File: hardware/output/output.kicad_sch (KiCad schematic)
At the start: 100 parts, among them J1 AudioJack2_SwitchT, J2 AudioJack2_SwitchT, J3 AudioJack2_SwitchT, J4 AudioJack2_SwitchT, J5 Conn_02x08_Odd_Even, J6 AudioJack3, J7 Conn_02x08_Odd_Even, J8 Conn_02x08_Odd_Even, Q1 2N3906, Q2 2N3904, Q3 2N3906, Q4 2N3904, U1 TL074, U2 LM386, U3 LM386

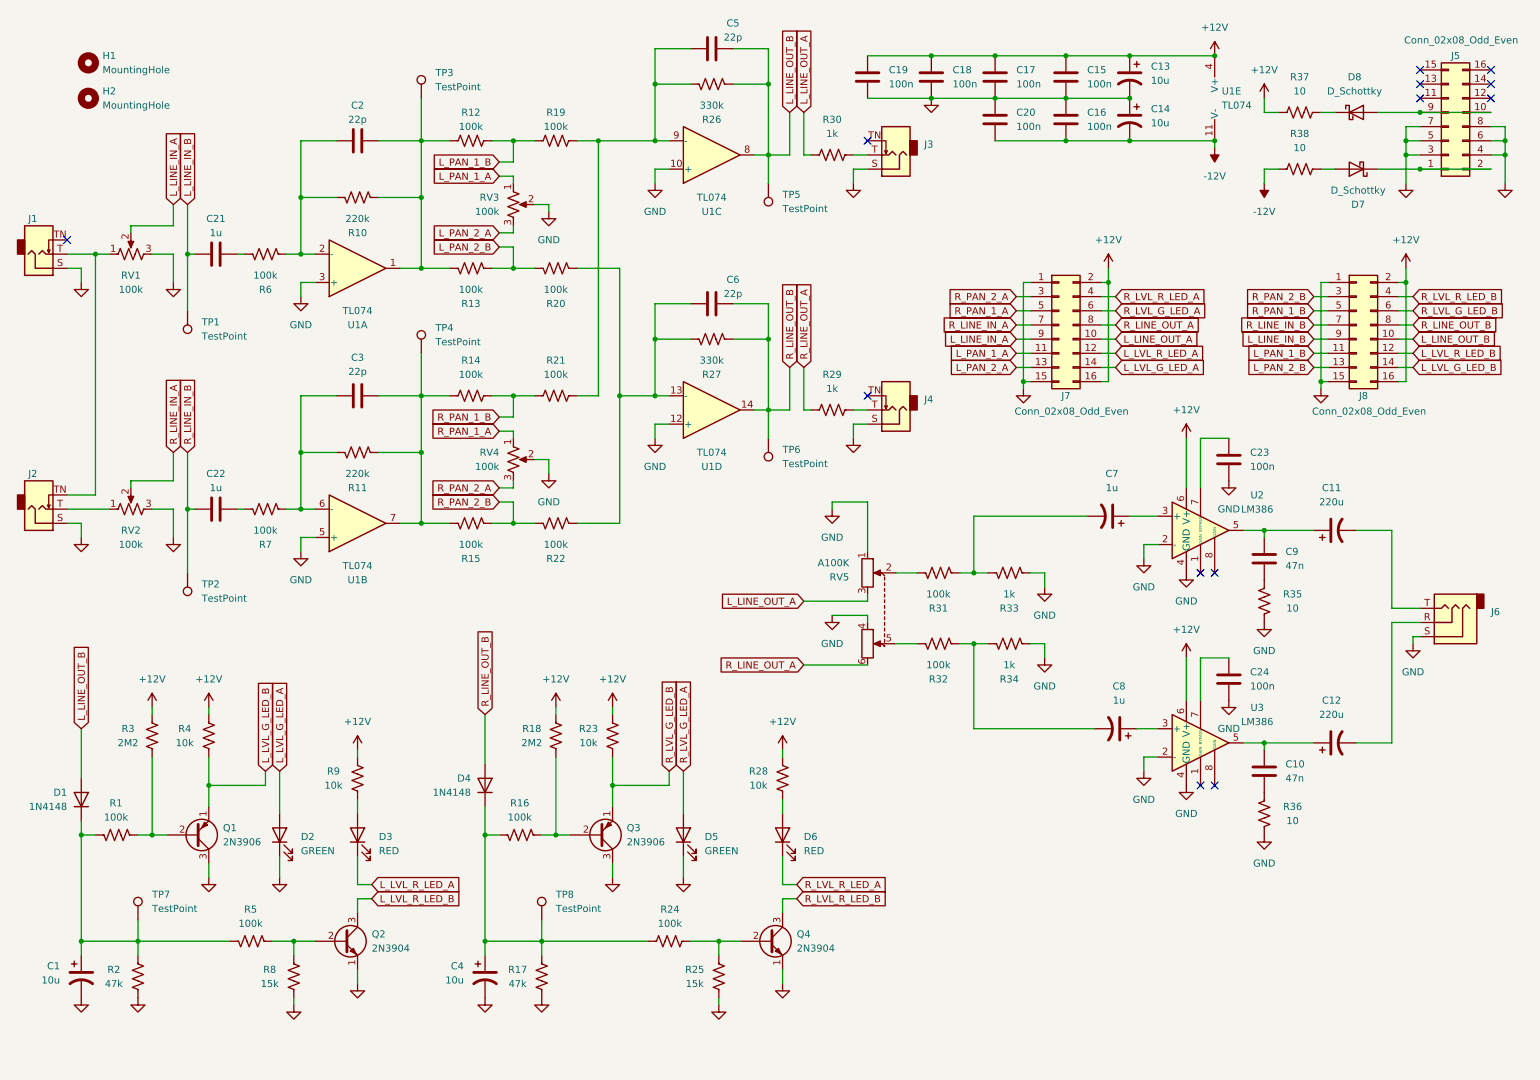
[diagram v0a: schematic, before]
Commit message: v2 board: SMT components, upgraded OPA1688 amplifier
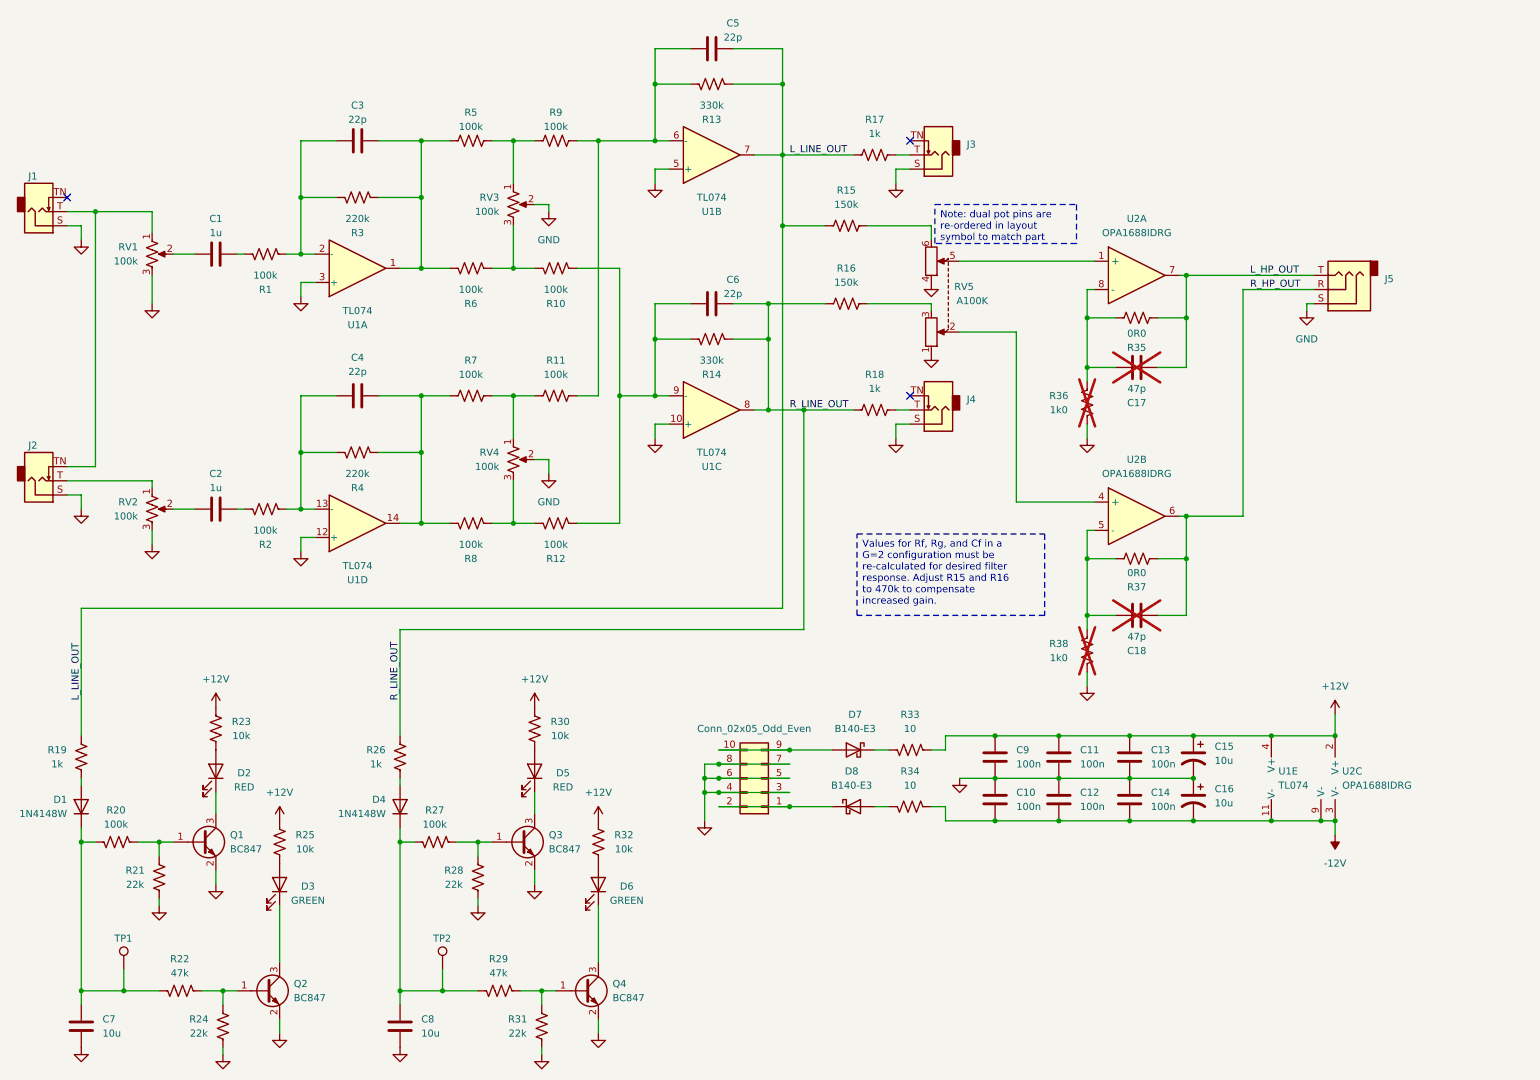
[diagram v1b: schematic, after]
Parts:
- removed C1, C4: 10u, Capacitor_THT:CP_Radial_D4.0mm_P2.00mm, symbol Device:C_Polarized_US
- removed C10, C9: 47n, Capacitor_THT:C_Disc_D5.0mm_W2.5mm_P2.50mm, symbol Device:C
- removed C11, C12: 220u, Capacitor_THT:CP_Radial_D6.3mm_P2.50mm, symbol Device:C_Polarized_US
- removed C23, C24: 100n, Capacitor_THT:C_Disc_D5.0mm_W2.5mm_P2.50mm, symbol Device:C
- removed C7: 1u, Capacitor_THT:C_Disc_D5.0mm_W2.5mm_P5.00mm, symbol Device:C_Polarized_US
- removed C8: 1u, Capacitor_THT:C_Disc_D5.0mm_W2.5mm_P2.50mm, symbol Device:C_Polarized_US
- removed D1: 1N4148, Diode_THT:D_DO-35_SOD27_P7.62mm_Horizontal, symbol Diode:1N4148
- removed D2: GREEN, LED_THT:LED_D3.0mm_Clear, symbol Device:LED
- removed D4: 1N4148, Diode_THT:D_DO-35_SOD27_P2.54mm_Vertical_AnodeUp, symbol Diode:1N4148
- removed D7, D8: D_Schottky, Diode_THT:D_DO-41_SOD81_P7.62mm_Horizontal, symbol Device:D_Schottky
- removed H1, H2: MountingHole, MountingHole:MountingHole_3.2mm_M3_DIN965, symbol Mechanical:MountingHole
- removed J5: Conn_02x08_Odd_Even, Connector_IDC:IDC-Header_2x08_P2.54mm_Vertical, symbol Connector_Generic:Conn_02x08_Odd_Even
- removed J7, J8: Conn_02x08_Odd_Even, Custom_PinHeader_P2.54mm:PinHeader_2x08_P2.54mm_Vertical_ThinPad, symbol Connector_Generic:Conn_02x08_Odd_Even
- removed Q1, Q3: 2N3906, Package_TO_SOT_THT:TO-92_Inline_Wide, symbol Transistor_BJT:2N3906
- removed Q2, Q4: 2N3904, Package_TO_SOT_THT:TO-92_Inline_Wide, symbol Transistor_BJT:2N3904
- removed R1: 100k, Resistor_THT:R_Axial_DIN0204_L3.6mm_D1.6mm_P2.54mm_Vertical, symbol Device:R_US
- removed R17, R2: 47k, Resistor_THT:R_Axial_DIN0204_L3.6mm_D1.6mm_P2.54mm_Vertical, symbol Device:R_US
- removed R18, R3: 2M2, Resistor_THT:R_Axial_DIN0204_L3.6mm_D1.6mm_P2.54mm_Vertical, symbol Device:R_US
- removed R23, R4: 10k, Resistor_THT:R_Axial_DIN0204_L3.6mm_D1.6mm_P2.54mm_Vertical, symbol Device:R_US
- removed R33, R34: 1k, Resistor_THT:R_Axial_DIN0204_L3.6mm_D1.6mm_P2.54mm_Vertical, symbol Device:R_US
- removed TP1, TP3, TP4, TP5, TP6, TP8: TestPoint, Connector_PinHeader_2.54mm:PinHeader_1x01_P2.54mm_Vertical, symbol Connector:TestPoint
- removed U2, U3: LM386, Package_DIP:DIP-8_W7.62mm_Socket, symbol Amplifier_Audio:LM386
- added C17, C18: 47p, Capacitor_SMD:C_0805_2012Metric_Pad1.18x1.45mm_HandSolder, symbol Device:C
- added C7, C8: 10u, Capacitor_SMD:C_0805_2012Metric_Pad1.18x1.45mm_HandSolder, symbol Device:C
- added D1, D4: 1N4148W, Diode_SMD:D_SOD-123, symbol Diode:1N4148W
- added D3: GREEN, LED_THT:LED_D3.0mm_Clear, symbol Device:LED
- added D7, D8: B140-E3, Diode_SMD:D_SMA, symbol Diode:B140-E3
- added J6: Conn_02x05_Odd_Even, Connector_IDC:IDC-Header_2x05_P2.54mm_Vertical, symbol Connector_Generic:Conn_02x05_Odd_Even
- added Q1, Q2, Q3, Q4: BC847, Package_TO_SOT_SMD:SOT-23, symbol Transistor_BJT:BC847
- added R15: 150k, Resistor_SMD:R_0805_2012Metric_Pad1.20x1.40mm_HandSolder, symbol Device:R_US
- added R19, R26: 1k, Resistor_SMD:R_0805_2012Metric_Pad1.20x1.40mm_HandSolder, symbol Device:R_US
- added R22, R29: 47k, Resistor_SMD:R_0805_2012Metric_Pad1.20x1.40mm_HandSolder, symbol Device:R_US
- added R27: 100k, Resistor_SMD:R_0805_2012Metric_Pad1.20x1.40mm_HandSolder, symbol Device:R_US
- added R30: 10k, Resistor_SMD:R_0805_2012Metric_Pad1.20x1.40mm_HandSolder, symbol Device:R_US
- added R37: 0R0, Resistor_SMD:R_0805_2012Metric_Pad1.20x1.40mm_HandSolder, symbol Device:R_US
- added R38: 1k0, Resistor_SMD:R_0805_2012Metric_Pad1.20x1.40mm_HandSolder, symbol Device:R_US
- added U2: OPA1688IDRG, Package_SON:WSON-8-1EP_3x3mm_P0.5mm_EP1.2x2mm, symbol AudioICs:OPA1688IDRG
- C1: renamed from C21; footprint Capacitor_THT:C_Disc_D5.0mm_W2.5mm_P2.50mm -> Capacitor_SMD:C_0805_2012Metric_Pad1.18x1.45mm_HandSolder
- C10: renamed from C19; footprint Capacitor_THT:C_Disc_D5.0mm_W2.5mm_P5.00mm -> Capacitor_SMD:C_0805_2012Metric_Pad1.18x1.45mm_HandSolder
- C11: renamed from C17; footprint Capacitor_THT:C_Disc_D5.0mm_W2.5mm_P2.50mm -> Capacitor_SMD:C_0805_2012Metric_Pad1.18x1.45mm_HandSolder
- C12: renamed from C20; footprint Capacitor_THT:C_Disc_D5.0mm_W2.5mm_P5.00mm -> Capacitor_SMD:C_0805_2012Metric_Pad1.18x1.45mm_HandSolder
- C13: renamed from C15; footprint Capacitor_THT:C_Disc_D5.0mm_W2.5mm_P2.50mm -> Capacitor_SMD:C_0805_2012Metric_Pad1.18x1.45mm_HandSolder
- C14: renamed from C16; footprint Capacitor_THT:C_Disc_D5.0mm_W2.5mm_P2.50mm -> Capacitor_SMD:C_0805_2012Metric_Pad1.18x1.45mm_HandSolder
- C15: renamed from C13; footprint Capacitor_THT:CP_Radial_D4.0mm_P2.00mm -> Capacitor_THT:CP_Radial_D5.0mm_P2.00mm
- C16: renamed from C14; footprint Capacitor_THT:CP_Radial_D4.0mm_P2.00mm -> Capacitor_THT:CP_Radial_D5.0mm_P2.00mm
- C2: renamed from C22; footprint Capacitor_THT:C_Disc_D5.0mm_W2.5mm_P2.50mm -> Capacitor_SMD:C_0805_2012Metric_Pad1.18x1.45mm_HandSolder
- C3: renamed from C2; footprint Capacitor_THT:C_Disc_D5.0mm_W2.5mm_P2.50mm -> Capacitor_SMD:C_0805_2012Metric_Pad1.18x1.45mm_HandSolder
- C4: renamed from C3; footprint Capacitor_THT:C_Disc_D5.0mm_W2.5mm_P2.50mm -> Capacitor_SMD:C_0805_2012Metric_Pad1.18x1.45mm_HandSolder
- C5, C6: footprint Capacitor_THT:C_Disc_D5.0mm_W2.5mm_P2.50mm -> Capacitor_SMD:C_0805_2012Metric_Pad1.18x1.45mm_HandSolder
- C9: renamed from C18; footprint Capacitor_THT:C_Disc_D5.0mm_W2.5mm_P2.50mm -> Capacitor_SMD:C_0805_2012Metric_Pad1.18x1.45mm_HandSolder
- D5: value GREEN -> RED
- D6: value RED -> GREEN
- J1, J2, J3, J4: footprint AudioJacks:Jack_3.5mm_QingPu_WQP-PJ301M-12_Vertical -> AudioJacks:Jack_3.5mm_QingPu_WQP-PJ301M-12_Vertical_Slim
- R1: renamed from R6; footprint Resistor_THT:R_Axial_DIN0207_L6.3mm_D2.5mm_P7.62mm_Horizontal -> Resistor_SMD:R_0805_2012Metric_Pad1.20x1.40mm_HandSolder
- R10: renamed from R20; footprint Resistor_THT:R_Axial_DIN0204_L3.6mm_D1.6mm_P2.54mm_Vertical -> Resistor_SMD:R_0805_2012Metric_Pad1.20x1.40mm_HandSolder
- R11: renamed from R21; footprint Resistor_THT:R_Axial_DIN0204_L3.6mm_D1.6mm_P2.54mm_Vertical -> Resistor_SMD:R_0805_2012Metric_Pad1.20x1.40mm_HandSolder
- R12: renamed from R22; footprint Resistor_THT:R_Axial_DIN0207_L6.3mm_D2.5mm_P7.62mm_Horizontal -> Resistor_SMD:R_0805_2012Metric_Pad1.20x1.40mm_HandSolder
- R13: renamed from R26; footprint Resistor_THT:R_Axial_DIN0204_L3.6mm_D1.6mm_P2.54mm_Vertical -> Resistor_SMD:R_0805_2012Metric_Pad1.20x1.40mm_HandSolder
- R14: renamed from R27; footprint Resistor_THT:R_Axial_DIN0204_L3.6mm_D1.6mm_P2.54mm_Vertical -> Resistor_SMD:R_0805_2012Metric_Pad1.20x1.40mm_HandSolder
- R16: value 100k -> 150k; footprint Resistor_THT:R_Axial_DIN0204_L3.6mm_D1.6mm_P2.54mm_Vertical -> Resistor_SMD:R_0805_2012Metric_Pad1.20x1.40mm_HandSolder
- R17: renamed from R30; footprint Resistor_THT:R_Axial_DIN0204_L3.6mm_D1.6mm_P2.54mm_Vertical -> Resistor_SMD:R_0805_2012Metric_Pad1.20x1.40mm_HandSolder
- R18: renamed from R29; footprint Resistor_THT:R_Axial_DIN0204_L3.6mm_D1.6mm_P2.54mm_Vertical -> Resistor_SMD:R_0805_2012Metric_Pad1.20x1.40mm_HandSolder
- R2: renamed from R7; footprint Resistor_THT:R_Axial_DIN0204_L3.6mm_D1.6mm_P2.54mm_Vertical -> Resistor_SMD:R_0805_2012Metric_Pad1.20x1.40mm_HandSolder
- R20: renamed from R5; footprint Resistor_THT:R_Axial_DIN0204_L3.6mm_D1.6mm_P2.54mm_Vertical -> Resistor_SMD:R_0805_2012Metric_Pad1.20x1.40mm_HandSolder
- R21: renamed from R8; value 15k -> 22k; footprint Resistor_THT:R_Axial_DIN0204_L3.6mm_D1.6mm_P2.54mm_Vertical -> Resistor_SMD:R_0805_2012Metric_Pad1.20x1.40mm_HandSolder
- R23: renamed from R9; footprint Resistor_THT:R_Axial_DIN0204_L3.6mm_D1.6mm_P2.54mm_Vertical -> Resistor_SMD:R_0805_2012Metric_Pad1.20x1.40mm_HandSolder
- R24, R31: value 100k -> 22k; footprint Resistor_THT:R_Axial_DIN0204_L3.6mm_D1.6mm_P2.54mm_Vertical -> Resistor_SMD:R_0805_2012Metric_Pad1.20x1.40mm_HandSolder
- R25: value 15k -> 10k; footprint Resistor_THT:R_Axial_DIN0204_L3.6mm_D1.6mm_P2.54mm_Vertical -> Resistor_SMD:R_0805_2012Metric_Pad1.20x1.40mm_HandSolder
- R28: value 10k -> 22k; footprint Resistor_THT:R_Axial_DIN0204_L3.6mm_D1.6mm_P2.54mm_Vertical -> Resistor_SMD:R_0805_2012Metric_Pad1.20x1.40mm_HandSolder
- R3: renamed from R10; footprint Resistor_THT:R_Axial_DIN0204_L3.6mm_D1.6mm_P2.54mm_Vertical -> Resistor_SMD:R_0805_2012Metric_Pad1.20x1.40mm_HandSolder
- R32: value 100k -> 10k; footprint Resistor_THT:R_Axial_DIN0204_L3.6mm_D1.6mm_P2.54mm_Vertical -> Resistor_SMD:R_0805_2012Metric_Pad1.20x1.40mm_HandSolder
- R33: renamed from R37; footprint Resistor_THT:R_Axial_DIN0207_L6.3mm_D2.5mm_P7.62mm_Horizontal -> Resistor_SMD:R_0805_2012Metric_Pad1.20x1.40mm_HandSolder
- R34: renamed from R38; footprint Resistor_THT:R_Axial_DIN0207_L6.3mm_D2.5mm_P7.62mm_Horizontal -> Resistor_SMD:R_0805_2012Metric_Pad1.20x1.40mm_HandSolder
- R35: value 10 -> 0R0; footprint Resistor_THT:R_Axial_DIN0204_L3.6mm_D1.6mm_P2.54mm_Vertical -> Resistor_SMD:R_0805_2012Metric_Pad1.20x1.40mm_HandSolder
- R36: value 10 -> 1k0; footprint Resistor_THT:R_Axial_DIN0204_L3.6mm_D1.6mm_P2.54mm_Vertical -> Resistor_SMD:R_0805_2012Metric_Pad1.20x1.40mm_HandSolder; now not fitted
- R4: renamed from R11; footprint Resistor_THT:R_Axial_DIN0204_L3.6mm_D1.6mm_P2.54mm_Vertical -> Resistor_SMD:R_0805_2012Metric_Pad1.20x1.40mm_HandSolder
- R5: renamed from R12; footprint Resistor_THT:R_Axial_DIN0204_L3.6mm_D1.6mm_P2.54mm_Vertical -> Resistor_SMD:R_0805_2012Metric_Pad1.20x1.40mm_HandSolder
- R6: renamed from R13; footprint Resistor_THT:R_Axial_DIN0204_L3.6mm_D1.6mm_P2.54mm_Vertical -> Resistor_SMD:R_0805_2012Metric_Pad1.20x1.40mm_HandSolder
- R7: renamed from R14; footprint Resistor_THT:R_Axial_DIN0207_L6.3mm_D2.5mm_P7.62mm_Horizontal -> Resistor_SMD:R_0805_2012Metric_Pad1.20x1.40mm_HandSolder
- R8: renamed from R15; footprint Resistor_THT:R_Axial_DIN0204_L3.6mm_D1.6mm_P2.54mm_Vertical -> Resistor_SMD:R_0805_2012Metric_Pad1.20x1.40mm_HandSolder
- R9: renamed from R19; footprint Resistor_THT:R_Axial_DIN0204_L3.6mm_D1.6mm_P2.54mm_Vertical -> Resistor_SMD:R_0805_2012Metric_Pad1.20x1.40mm_HandSolder
- TP1: renamed from TP7; footprint Connector_PinHeader_2.54mm:PinHeader_1x01_P2.54mm_Vertical -> TestPoint:TestPoint_Pad_D1.5mm
- TP2: footprint Connector_PinHeader_2.54mm:PinHeader_1x01_P2.54mm_Vertical -> TestPoint:TestPoint_Pad_D1.5mm
- U1: footprint Package_DIP:DIP-14_W7.62mm_Socket -> Package_SO:SOIC-14_3.9x8.7mm_P1.27mm
- renumbered D3 to D2, J6 to J5
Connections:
- net L_LINE_IN_B is gone; now on an unnamed net: C1.1
- net L_PAN_1_B is gone; now on an unnamed net: R5.2, R9.1
- net L_PAN_2_B is gone; now on an unnamed net: R10.1, R6.2
- net R_PAN_1_B is gone; now on an unnamed net: R11.1, R7.2
- net R_PAN_2_B is gone; now on an unnamed net: R12.1, R8.2
- net +12V: now also R23.1, R25.1, R32.1, R30.1, U2.2 (V+); no longer C10.2, R23.2, R28.2
- net -12V: now also C10.1, U2.3 (V-), U2.9 (V-)
- net GND: now also C10.2, R24.1, R28.1, R31.1, R36.2, C7.1, C8.1, J6.3 (Pin_3), J6.4 (Pin_4), J6.5 (Pin_5), J6.6 (Pin_6), J6.7 (Pin_7), J6.8 (Pin_8), Q1.2 (E), Q2.2 (E), Q3.2 (E), Q4.2 (E), R38.2; no longer C10.1, D5.1 (K), R25.1, R35.1, R36.1
- net at R32.2: now also D6.2 (A)
- net R_LINE_OUT: now reaches R16.1
- net R_LINE_OUT: now also C6.2, R14.2, R18.1, U1.8, R26.2
- net at R16.2: now also RV5.3; no longer R24.1
- net at R20.2, TP1.1: now also C7.2, D1.1 (K), R22.2
- net at C5.1, R11.2, R13.1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: now also U1.6 (-); no longer U1.9 (-)
- net at C6.1, R10.2, R12.2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: now also U1.9 (-); no longer U1.13 (-)
- net at R35.2: now also R36.1, C17.1, U2.8 (-)
- net at RV5.2: now also U2.4 (+); no longer R31.1
- net at R31.2: now also Q4.1 (B), R29.1
- net at RV5.5: now also U2.1 (+); no longer R32.1
- net at R34.2: now also D8.2 (A)
- net at R24.2: now also Q2.1 (B), R22.1; no longer R25.2
- net at R20.1, R21.2: now also Q1.1 (B)
- net at D2.2 (A): now also R23.2; no longer R23.1
- net at C4.2, R4.2, R7.1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: now also U1.14; no longer U1.7
- net at C4.1, R2.2, R4.1: now also U1.13 (-); no longer U1.6 (-)
- net R_HP_OUT: now reaches J5.R
- net R_HP_OUT: now also C18.2, R37.1, U2.6
- net L_HP_OUT: now reaches J5.T
- net L_HP_OUT: now also R35.1, C17.2, U2.7
- net at R33.2: now also D7.1 (K)
- net L_LINE_IN_A: no longer names the net of RV1.2
- net L_LINE_OUT_A renamed L_LINE_OUT
- net L_LINE_OUT: now also C5.2, R13.2, U1.7, R15.1, R19.2; no longer RV5.3
- removed net L_LINE_OUT_B: C5.2, R13.2, U1.8
- net L_LVL_R_LED_A: no longer names the net of D2.1 (K)
- net L_LVL_R_LED_A: now also Q1.3 (C)
- net L_PAN_1_A: no longer names the net of RV3.1
- net L_PAN_2_A: no longer names the net of RV3.3
- net R_LINE_IN_A: no longer names the net of RV2.2
- net R_LINE_IN_A: now also C2.1
- net R_LINE_IN_B: no longer names the net of TP2.1
- net R_LINE_IN_B: now also C8.2, D4.1 (K), R27.2, R29.2; no longer C2.1
- net R_LINE_OUT_A: no longer names the net of RV5.6
- net R_LINE_OUT_A: now also R15.2; no longer R18.1
- removed net R_LINE_OUT_B: C6.2, R14.2, U1.14
- net R_LVL_G_LED_A: no longer names the net of D5.2 (A)
- net R_LVL_G_LED_A: now also R30.2
- net R_LVL_R_LED_A: no longer names the net of D6.1 (K)
- net R_LVL_R_LED_A: now also Q4.3 (C)
- net R_PAN_1_A: no longer names the net of RV4.1
- net R_PAN_2_A: no longer names the net of RV4.3
- new net: D4.2 (A), R26.1
- new net: Q3.1 (B), R27.1, R28.2
- new net: C18.1, R37.2, R38.1, U2.5 (-)
- new net: D3.1 (K), Q2.3 (C)
- new net: D1.2 (A), R19.1
- new net: D5.1 (K), Q3.3 (C)
- new net: D8.1 (K), J6.1 (Pin_1), J6.2 (Pin_2)
- new net: D7.2 (A), J6.10 (Pin_10), J6.9 (Pin_9)
- new net: D3.2 (A), R25.2
- no-connect marks 13 -> 3
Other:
- title: OUTPUT-1 -> Output
- moved on the sheet: C10, C11, C12, C13, C14, C15, C16, C9, D2, J1, J2, J3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
